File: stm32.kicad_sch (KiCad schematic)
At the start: 17 parts, among them J2 Conn_02x03_Odd_Even, J3 Conn_01x04, SW1 TS-1187A-B-A-B, U3 STM32F103C8T6

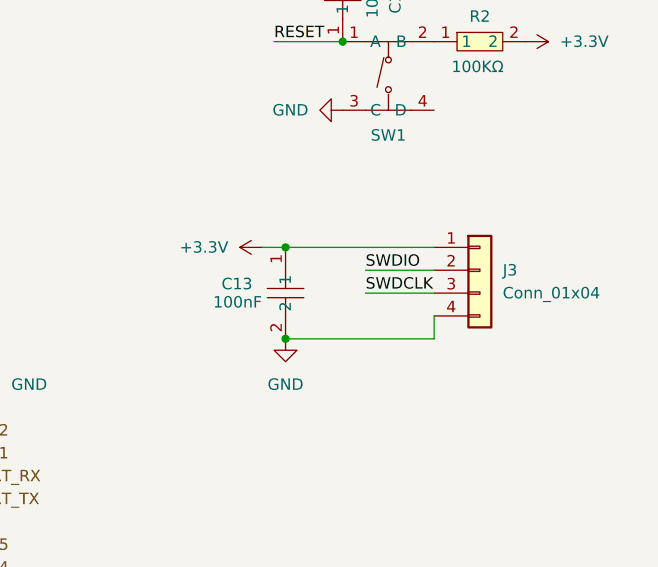
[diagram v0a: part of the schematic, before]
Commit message: changed IMU, reworked PCB layout
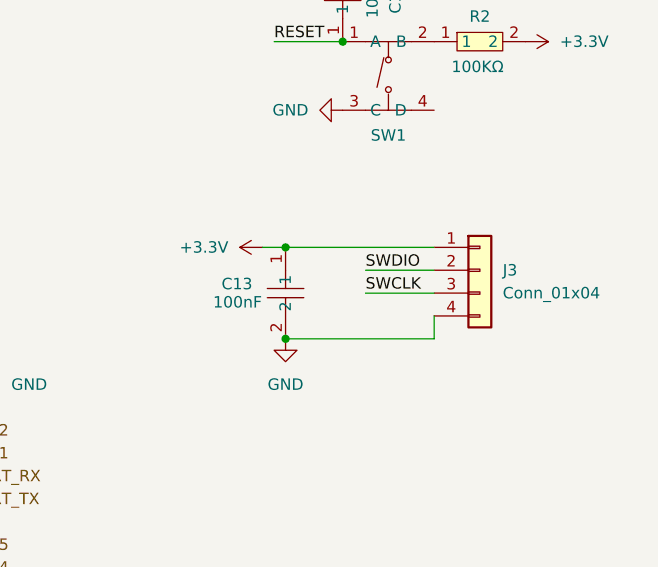
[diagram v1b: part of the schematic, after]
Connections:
- net SWDCLK is gone; now on net SWCLK: J3.3 (Pin_3)
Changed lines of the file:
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@@
 		)
 	)
-	(label "SWDCLK"
+	(label "SWCLK"
 		(at 161.29 96.52 0)
 		(effects

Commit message: more work
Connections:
- net +3.3V: now also J3.4 (Pin_4); no longer J3.1 (Pin_1)
- net GND: now also J3.1 (Pin_1), SW1.1 (A); no longer J3.4 (Pin_4), SW1.3 (C)
- net RESET: now also SW1.3 (C); no longer SW1.1 (A)
- net SWCLK: now also J3.2 (Pin_2); no longer J3.3 (Pin_3)
- net SWDIO: now also J3.3 (Pin_3); no longer J3.2 (Pin_2)
- net at R2.1: now also SW1.4 (D); no longer SW1.2 (B)
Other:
- moved on the sheet: C13, C14, R2, SW1

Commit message: Finished pcb
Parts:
- removed R25, R26: 0603WAF1002T5E, easyeda2kicad:R0603, symbol lol:0603WAF1002T5E
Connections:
- net PC13: now reaches U3.2 (PC13-TAMPER-RTC)
- net PC14: now reaches U3.3 (PC14-OSC32_IN)
- net PC15: now reaches U3.4 (PC15-OSC32_OUT)
- net PD0: now reaches U3.5 (PD0-OSC_IN)
- net PD1: now reaches U3.6 (PD1-OSC_OUT)
